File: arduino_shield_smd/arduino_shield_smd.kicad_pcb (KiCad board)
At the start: 2 copper layers, 68.6 x 53.3 mm, 51 parts, among them J1 Power, J2 Digital/PWM, J3 Analog, J4 Digital/PWM, J5 1X5 2.5mm, J6 1x2 2.5mm, U1 PCF8574T, U2 ULN2803A, U3 PCF8574T, U4 ULN2803A

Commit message: Tweak paths
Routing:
- net VIN: track 151.8 -> 153.3 mm, vias 2 -> 1
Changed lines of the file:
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@@
 		(start 163.8 109.3)
 		(end 162.93 109.3)
-		(width 0.25)
+		(width 0.4)
 		(layer "F.Cu")
 		(net 3)
@@
 		(start 162.93 109.3)
 		(end 157 103.37)
-		(width 0.25)
+		(width 0.4)
 		(layer "F.Cu")
 		(net 3)
@@
 	)
 	(segment
-		(start 177.1 123)
-		(end 177.1 120.375)
+		(start 164.3 123.6)
+		(end 174.4 123.6)
 		(width 0.25)
 		(layer "F.Cu")
@@
 	)
 	(segment
+		(start 174.4 123.6)
+		(end 178.875 119.125)
+		(width 0.25)
+		(layer "F.Cu")
+		(net 8)
+	)
+	(segment
 		(start 158.67 129.25)
 		(end 160.42 127.5)
@@
 	)
 	(segment
-		(start 140.766509 107.1)
-		(end 140.726509 107.14)
-		(width 0.25)
-		(layer "F.Cu")
-		(net 8)
-	)
-	(segment
 		(start 129.839999 111.15)
 		(end 131.72 111.15)
@@
 	)
 	(segment
-		(start 140.726509 107.14)
-		(end 134.2 107.14)
-		(width 0.25)
-		(layer "F.Cu")
-		(net 8)
-	)
-	(segment
 		(start 123.3 124.1)
 		(end 123.9 123.5)
@@
 	)
 	(segment
+		(start 178.875 119.125)
+		(end 178.875 118.6)
+		(width 0.25)
+		(layer "F.Cu")
+		(net 8)
+	)
+	(segment
 		(start 131.7 127.4)
 		(end 133.55 129.25)
@@
 	)
 	(segment
-		(start 177.1 120.375)
-		(end 178.875 118.6)
-		(width 0.25)
-		(layer "F.Cu")
-		(net 8)
-	)
-	(segment
 		(start 131.8 86.1)
 		(end 131.8 107)
@@
 	)
 	(segment
-		(start 176.3 123.8)
-		(end 177.1 123)
-		(width 0.25)
-		(layer "F.Cu")
-		(net 8)
-	)
-	(segment
 		(start 123.9 125.5)
 		(end 123.9 123.5)
@@
 	)
 	(via
-		(at 140.766509 107.1)
+		(at 164.3 123.6)
 		(size 0.8)
 		(drill 0.4)
@@
 		(net 8)
 	)
-	(via
-		(at 176.3 123.8)
-		(size 0.8)
-		(drill 0.4)
-		(layers "F.Cu" "B.Cu")
-		(free yes)
-		(net 8)
-	)
-	(segment
-		(start 174.4 128.2)
-		(end 173.75 128.85)
-		(width 0.25)
-		(layer "B.Cu")
-		(net 8)
-	)
-	(segment
-		(start 173.75 128.85)
-		(end 161.77 128.85)
+	(segment
+		(start 164.3 123.6)
+		(end 164.3 123.62)
+		(width 0.25)
+		(layer "B.Cu")
+		(net 8)
+	)
+	(segment
+		(start 164.3 123.62)
+		(end 160.42 127.5)
 		(width 0.25)
 		(layer "B.Cu")
@@
 	(segment
 		(start 157 96.37)
-		(end 155.63 96.37)
-		(width 0.25)
-		(layer "B.Cu")
-		(net 8)
-	)
-	(segment
-		(start 174.4 125.7)
-		(end 174.4 128.2)
-		(width 0.25)
-		(layer "B.Cu")
-		(net 8)
-	)
-	(segment
-		(start 176.3 123.8)
-		(end 174.4 125.7)
-		(width 0.25)
-		(layer "B.Cu")
-		(net 8)
-	)
-	(segment
-		(start 155.63 96.37)
-		(end 144.9 107.1)
-		(width 0.25)
-		(layer "B.Cu")
-		(net 8)
-	)
-	(segment
-		(start 144.9 107.1)
-		(end 140.766509 107.1)
-		(width 0.25)
-		(layer "B.Cu")
-		(net 8)
-	)
-	(segment
-		(start 161.77 128.85)
+		(end 160.42 99.79)
+		(width 0.4)
+		(layer "B.Cu")
+		(net 8)
+	)
+	(segment
+		(start 160.42 99.79)
 		(end 160.42 127.5)
-		(width 0.25)
+		(width 0.4)
 		(layer "B.Cu")
 		(net 8)
@@
 	)
 	(segment
-		(start 175.7 99.9)
-		(end 177.1 101.3)
+		(start 177.3 101.1)
+		(end 177.3 107.7)
 		(width 0.25)
 		(layer "B.Cu")
@@
 	)
 	(segment
-		(start 177.1 101.3)
-		(end 177.1 107.5)
+		(start 176.1 99.9)
+		(end 177.3 101.1)
+		(width 0.25)
+		(layer "B.Cu")
+		(net 15)
+	)
+	(segment
+		(start 177.3 107.7)
+		(end 179.3 109.7)
 		(width 0.25)
 		(layer "B.Cu")
@@
 	)
 	(segment
-		(start 173.4 99.9)
-		(end 175.7 99.9)
-		(width 0.25)
-		(layer "B.Cu")
-		(net 15)
-	)
-	(segment
-		(start 177.1 107.5)
-		(end 179.3 109.7)
-		(width 0.25)
-		(layer "B.Cu")
-		(net 15)
-	)
-	(segment
 		(start 166.3 92.8)
 		(end 173.4 99.9)
@@
 	)
 	(segment
+		(start 173.4 99.9)
+		(end 176.1 99.9)
+		(width 0.25)
+		(layer "B.Cu")
+		(net 15)
+	)
+	(segment
 		(start 153.816 79.24)
 		(end 157 82.424)
@@
 	)
 	(segment
-		(start 176.1 99.2)
-		(end 177.8 100.9)
+		(start 178 100.8)
+		(end 178 102.9)
+		(width 0.25)
+		(layer "B.Cu")
+		(net 17)
+	)
+	(segment
+		(start 178 102.9)
+		(end 179.3 104.2)
+		(width 0.25)
+		(layer "B.Cu")
+		(net 17)
+	)
+	(segment
+		(start 176.4 99.2)
+		(end 178 100.8)
+		(width 0.25)
+		(layer "B.Cu")
+		(net 17)
+	)
+	(segment
+		(start 165.5 79.24)
+		(end 167.5 81.24)
+		(width 0.25)
+		(layer "B.Cu")
+		(net 17)
+	)
+	(segment
+		(start 167.5 81.24)
+		(end 167.5 92.2)
 		(width 0.25)
 		(layer "B.Cu")
@@
 	)
 	(segment
-		(start 177.8 102.7)
-		(end 179.3 104.2)
-		(width 0.25)
-		(layer "B.Cu")
-		(net 17)
-	)
-	(segment
-		(start 177.8 100.9)
-		(end 177.8 102.7)
-		(width 0.25)
-		(layer "B.Cu")
-		(net 17)
-	)
-	(segment
 		(start 174.5 99.2)
-		(end 176.1 99.2)
-		(width 0.25)
-		(layer "B.Cu")
-		(net 17)
-	)
-	(segment
-		(start 167.5 81.24)
-		(end 167.5 92.2)
-		(width 0.25)
-		(layer "B.Cu")
-		(net 17)
-	)
-	(segment
-		(start 165.5 79.24)
-		(end 167.5 81.24)
-		(width 0.25)
-		(layer "B.Cu")
+		(end 176.4 99.2)
+		(width 0.25)
+		(layer "B.Cu")

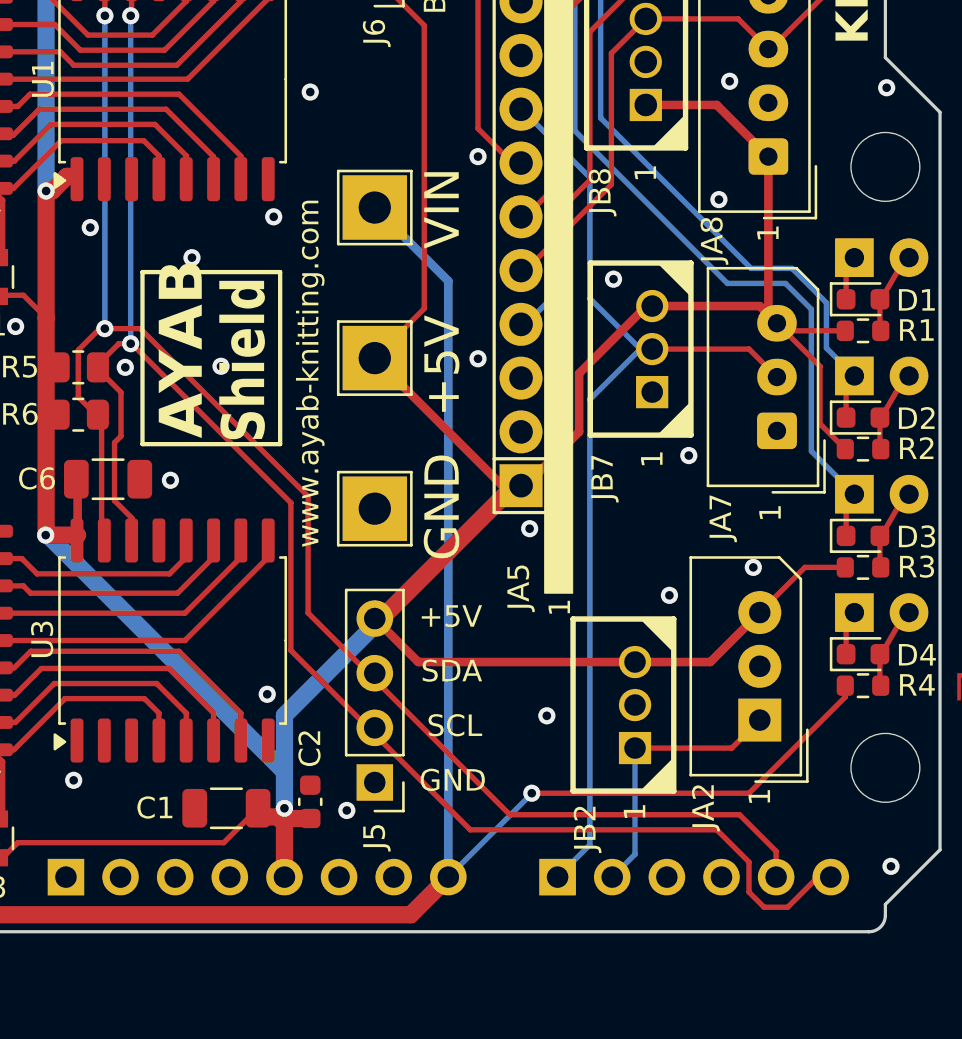
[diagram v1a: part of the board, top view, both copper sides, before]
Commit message: Tweak ground plane
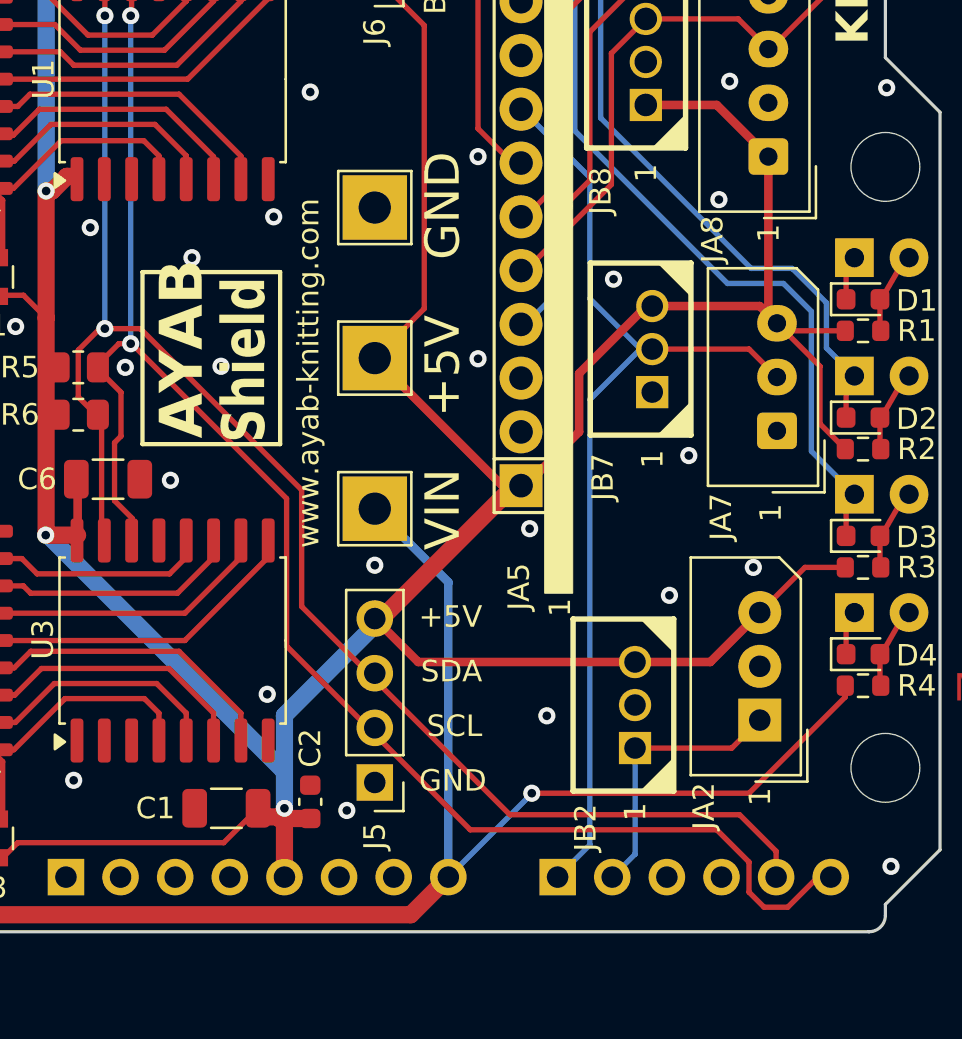
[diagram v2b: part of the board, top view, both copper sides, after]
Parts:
- moved TP1 14.0 mm to (157.0, 96.4)
- moved TP3 14.0 mm to (157.0, 110.4)
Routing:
- net VIN: track 153.3 -> 139.3 mm
- net GND: vias 48 -> 49
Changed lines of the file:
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@@
 	(footprint "TestPoint:TestPoint_THTPad_3.0x3.0mm_Drill1.5mm"
 		(layer "F.Cu")
-		(at 157 96.37)
+		(at 157 110.37)
 		(descr "THT rectangular pad as test Point, square 3.0mm side length, hole diameter 1.5mm")
 		(tags "test point THT pad rectangle square")
@@
 	(footprint "TestPoint:TestPoint_THTPad_3.0x3.0mm_Drill1.5mm"
 		(layer "F.Cu")
-		(at 157 110.37)
+		(at 157 96.37)
 		(descr "THT rectangular pad as test Point, square 3.0mm side length, hole diameter 1.5mm")
 		(tags "test point THT pad rectangle square")
@@
 	)
 	(gr_text "GND"
-		(at 161.1 112.8 90)
+		(at 161.1 98.8 90)
 		(layer "F.SilkS")
 		(effects
@@
 	)
 	(gr_text "VIN"
-		(at 161.1 98.3 90)
+		(at 161.1 112.3 90)
 		(layer "F.SilkS")
 		(effects
@@
 	)
 	(via
+		(at 157 113)
+		(size 0.8)
+		(drill 0.4)
+		(layers "F.Cu" "B.Cu")
+		(free yes)
+		(net 2)
+	)
+	(via
 		(at 116 126)
 		(size 0.8)
@@
 	)
 	(segment
-		(start 157 96.37)
-		(end 160.42 99.79)
+		(start 160.42 113.79)
+		(end 157 110.37)
 		(width 0.4)
 		(layer "B.Cu")
@@
 	)
 	(segment
-		(start 160.42 99.79)
-		(end 160.42 127.5)
+		(start 160.42 127.5)
+		(end 160.42 113.79)
 		(width 0.4)
 		(layer "B.Cu")
@@
 	)
 	(segment
-		(start 144.45 102)
-		(end 146.1 102)
+		(start 153.6 109.5)
+		(end 153.6 114.92)
 		(width 0.25)
 		(layer "F.Cu")
@@
 	)
 	(segment
-		(start 173.962081 124.6)
-		(end 175.66 126.297919)
-		(width 0.25)
-		(layer "F.Cu")
-		(net 9)
-	)
-	(segment
-		(start 153.9 115.22)
-		(end 157 118.32)
-		(width 0.25)
-		(layer "F.Cu")
-		(net 9)
-	)
-	(segment
 		(start 144.3 106.26125)
 		(end 143.21375 105.175)
@@
 	)
 	(segment
-		(start 144.3 111.444999)
-		(end 144.3 106.26125)
+		(start 146.1 102)
+		(end 153.6 109.5)
 		(width 0.25)
 		(layer "F.Cu")
@@
 	)
 	(segment
-		(start 163.28 124.6)
-		(end 173.962081 124.6)
+		(start 144.3 111.444999)
+		(end 144.3 106.26125)
 		(width 0.25)
 		(layer "F.Cu")
@@
 	)
 	(segment
-		(start 144.4525 87.4525)
-		(end 144.4525 85.7775)
+		(start 163.28 124.6)
+		(end 173.962081 124.6)
 		(width 0.25)
 		(layer "F.Cu")
@@
 	)
 	(segment
-		(start 146.1 102)
-		(end 153.9 109.8)
+		(start 144.4525 87.4525)
+		(end 144.4525 85.7775)
 		(width 0.25)
 		(layer "F.Cu")
@@
 	)
 	(segment
-		(start 143.21375 105.175)
-		(end 143.21375 103)
-		(width 0.25)
-		(layer "F.Cu")
-		(net 9)
-	)
-	(segment
-		(start 153.9 109.8)
-		(end 153.9 115.22)
+		(start 173.962081 124.6)
+		(end 175.66 126.297919)
 		(width 0.25)
 		(layer "F.Cu")
@@
 	)
 	(segment
-		(start 157 118.32)
-		(end 163.28 124.6)
+		(start 143.21375 105.175)
+		(end 143.21375 103)
 		(width 0.25)
 		(layer "F.Cu")
@@
 	)
 	(segment
+		(start 153.6 114.92)
+		(end 163.28 124.6)
+		(width 0.25)
+		(layer "F.Cu")
+		(net 9)
+	)
+	(segment
 		(start 137.796 81)
 		(end 143.4 81)
@@
 		(net 9)
 	)
+	(segment
+		(start 144.45 102)
+		(end 146.1 102)
+		(width 0.25)
+		(layer "F.Cu")
+		(net 9)
+	)
 	(via
 		(at 144.45 102)
@@
 	)
 	(segment
-		(start 161.44 125.3)
-		(end 172.9 125.3)
-		(width 0.25)
-		(layer "F.Cu")
-		(net 10)
-	)
-	(segment
 		(start 145.725001 110.825001)
 		(end 145.725001 111.6)
@@
 	)
 	(segment
-		(start 175.1 128.9)
-		(end 176.2 128.9)
-		(width 0.25)
-		(layer "F.Cu")
-		(net 10)
-	)
-	(segment
 		(start 141.7 77.9)
 		(end 142.4 78.6)
@@
 	)
 	(segment
-		(start 176.2 128.9)
-		(end 177.6 127.5)
+		(start 145.7 102.7)
+		(end 145.6525 102.7)
 		(width 0.25)
 		(layer "F.Cu")
@@
 	)
 	(segment
-		(start 153.1 116.96)
-		(end 153.1 110.1)
+		(start 133.496 79.24)
+		(end 134.836 77.9)
 		(width 0.25)
 		(layer "F.Cu")
@@
 	)
 	(segment
-		(start 133.496 79.24)
-		(end 134.836 77.9)
+		(start 172.9 125.3)
+		(end 161.44 125.3)
 		(width 0.25)
 		(layer "F.Cu")
@@
 	)
 	(segment
-		(start 157 120.86)
-		(end 161.44 125.3)
+		(start 176.2 128.9)
+		(end 175.1 128.9)
 		(width 0.25)
 		(layer "F.Cu")
@@
 	)
 	(segment
-		(start 144.03875 103.76125)
-		(end 144.03875 103.8)
+		(start 175.1 128.9)
+		(end 174.4 128.2)
 		(width 0.25)
 		(layer "F.Cu")
@@
 	)
 	(segment
-		(start 153.1 110.1)
-		(end 145.7 102.7)
+		(start 174.4 126.8)
+		(end 172.9 125.3)
 		(width 0.25)
 		(layer "F.Cu")
@@
 	)
 	(segment
-		(start 144.9 107.3)
-		(end 144.9 110)
+		(start 152.9 116.76)
+		(end 152.9 109.9)
 		(width 0.25)
 		(layer "F.Cu")
@@
 	)
 	(segment
-		(start 143.1 80.5)
-		(end 143.7 80.5)
+		(start 144.03875 103.76125)
+		(end 144.03875 103.8)
 		(width 0.25)
 		(layer "F.Cu")
@@
 	)
 	(segment
-		(start 145.6525 102.7)
-		(end 145.1 102.7)
+		(start 144.9 107.3)
+		(end 144.9 110)
 		(width 0.25)
 		(layer "F.Cu")
@@
 	)
 	(segment
-		(start 145.7 102.7)
-		(end 145.6525 102.7)
+		(start 174.4 128.2)
+		(end 174.4 126.8)
 		(width 0.25)
 		(layer "F.Cu")
@@
 	)
 	(segment
-		(start 174.4 126.8)
-		(end 174.4 128.2)
+		(start 143.1 80.5)
+		(end 143.7 80.5)
 		(width 0.25)
 		(layer "F.Cu")
@@
 	)
 	(segment
-		(start 177.6 127.5)
-		(end 178.2 127.5)
+		(start 145.6525 102.7)
+		(end 145.1 102.7)
 		(width 0.25)
 		(layer "F.Cu")
@@
 	)
 	(segment
-		(start 157 120.86)
-		(end 153.1 116.96)
+		(start 145.695 84.995)
+		(end 145.695 85.75)
 		(width 0.25)
 		(layer "F.Cu")
@@
 	)
 	(segment
-		(start 145.695 84.995)
-		(end 145.695 85.75)
+		(start 178.2 127.5)
+		(end 177.6 127.5)
 		(width 0.25)
 		(layer "F.Cu")
@@
 	)
 	(segment
-		(start 144.9 84.2)
-		(end 145.695 84.995)
+		(start 177.6 127.5)
+		(end 176.2 128.9)
 		(width 0.25)
 		(layer "F.Cu")
@@
 	)
 	(segment
-		(start 145.2 104.96125)
-		(end 145.2 107)
+		(start 161.44 125.3)
+		(end 152.9 116.76)
 		(width 0.25)
 		(layer "F.Cu")
@@
 	)
 	(segment
-		(start 174.4 128.2)
-		(end 175.1 128.9)
+		(start 144.9 84.2)
+		(end 145.695 84.995)
+		(width 0.25)
+		(layer "F.Cu")
+		(net 10)
+	)
+	(segment
+		(start 145.2 104.96125)
+		(end 145.2 107)
 		(width 0.25)
 		(layer "F.Cu")
@@
 	)
 	(segment
-		(start 142.4 78.6)
-		(end 142.4 79.8)
+		(start 152.9 109.9)
+		(end 145.7 102.7)
 		(width 0.25)
 		(layer "F.Cu")
@@
 	)
 	(segment
-		(start 172.9 125.3)
-		(end 174.4 126.8)
+		(start 142.4 78.6)
+		(end 142.4 79.8)
 		(width 0.25)
 		(layer "F.Cu")
@@
 	)
 	(segment
-		(start 177.3 101.1)
-		(end 177.3 107.7)
+		(start 176 99.9)
+		(end 177.3 101.2)
 		(width 0.25)
 		(layer "B.Cu")
@@
 	)
 	(segment
-		(start 176.1 99.9)
-		(end 177.3 101.1)
+		(start 166.3 92.8)
+		(end 173.4 99.9)
 		(width 0.25)
 		(layer "B.Cu")
@@
 	)
 	(segment
-		(start 177.3 107.7)
-		(end 179.3 109.7)
+		(start 177.3 101.2)
+		(end 177.3 107.7)
 		(width 0.25)
 		(layer "B.Cu")
@@
 	)
 	(segment
-		(start 166.3 82.58)
-		(end 166.3 92.8)
+		(start 173.4 99.9)
+		(end 176 99.9)
 		(width 0.25)
 		(layer "B.Cu")
@@
 	)
 	(segment
-		(start 162.96 79.24)
-		(end 166.3 82.58)
+		(start 177.3 107.7)
+		(end 179.3 109.7)
 		(width 0.25)
 		(layer "B.Cu")
@@
 	)
 	(segment
-		(start 166.3 92.8)
-		(end 173.4 99.9)
+		(start 166.3 82.58)
+		(end 166.3 92.8)
 		(width 0.25)
 		(layer "B.Cu")
@@
 	)
 	(segment
-		(start 173.4 99.9)
-		(end 176.1 99.9)
+		(start 162.96 79.24)
+		(end 166.3 82.58)
 		(width 0.25)
 		(layer "B.Cu")
@@
 		(net 0)
 		(net_name "")
+		(locked yes)
 		(layer "F.Cu")
 		(hatch edge 0.5)
@@
 			)
 		)
+	)
+	(zone
+		(net 0)
+		(net_name "")
+		(locked yes)
+		(layer "F.Cu")
+		(hatch edge 0.5)
+		(connect_pads
+			(clearance 0)
+		)
+		(min_thickness 0.5)
+		(filled_areas_thickness no)
+		(keepout
+			(tracks allowed)
+			(vias allowed)
+			(pads allowed)
+			(copperpour not_allowed)
+			(footprints allowed)
+		)
+		(placement
+			(enabled no)
+			(sheetname "")
+		)
+		(fill
+			(thermal_gap 0.5)
+			(thermal_bridge_width 0.75)
+		)
+		(polygon
+			(pts
+				(xy 132 76.7) (xy 131.990871 81.2) (xy 180 81.2) (xy 180 76.7)
+			)
+		)
